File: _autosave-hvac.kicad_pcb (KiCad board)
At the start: 2 copper layers, 191.8 x 114.3 mm, 44 parts, among them IC1 ATMEGA328P-A, J1 PROGRAMMING HEADER, J2 SERIAL PORT, J3 POWER_INPUT, SW1 SPST, SW2 SPST, SW3 SPST, U1 MIC5225, U2 MOSFET_N, U3 MOSFET_N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

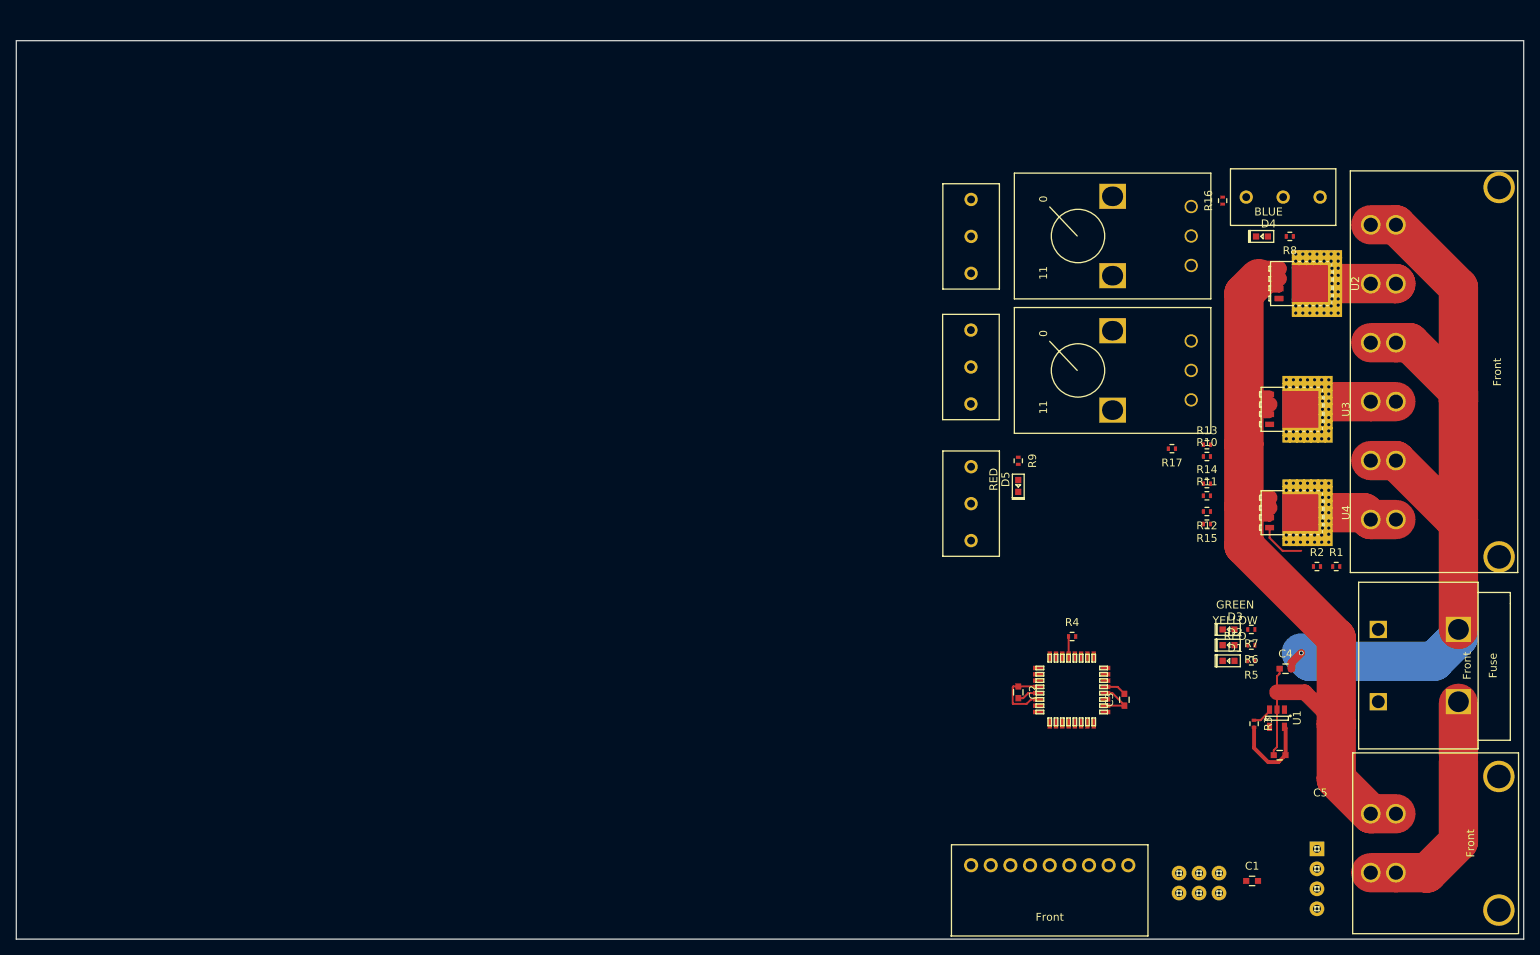
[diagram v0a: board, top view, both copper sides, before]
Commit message: Create hole footprint and route a few small things
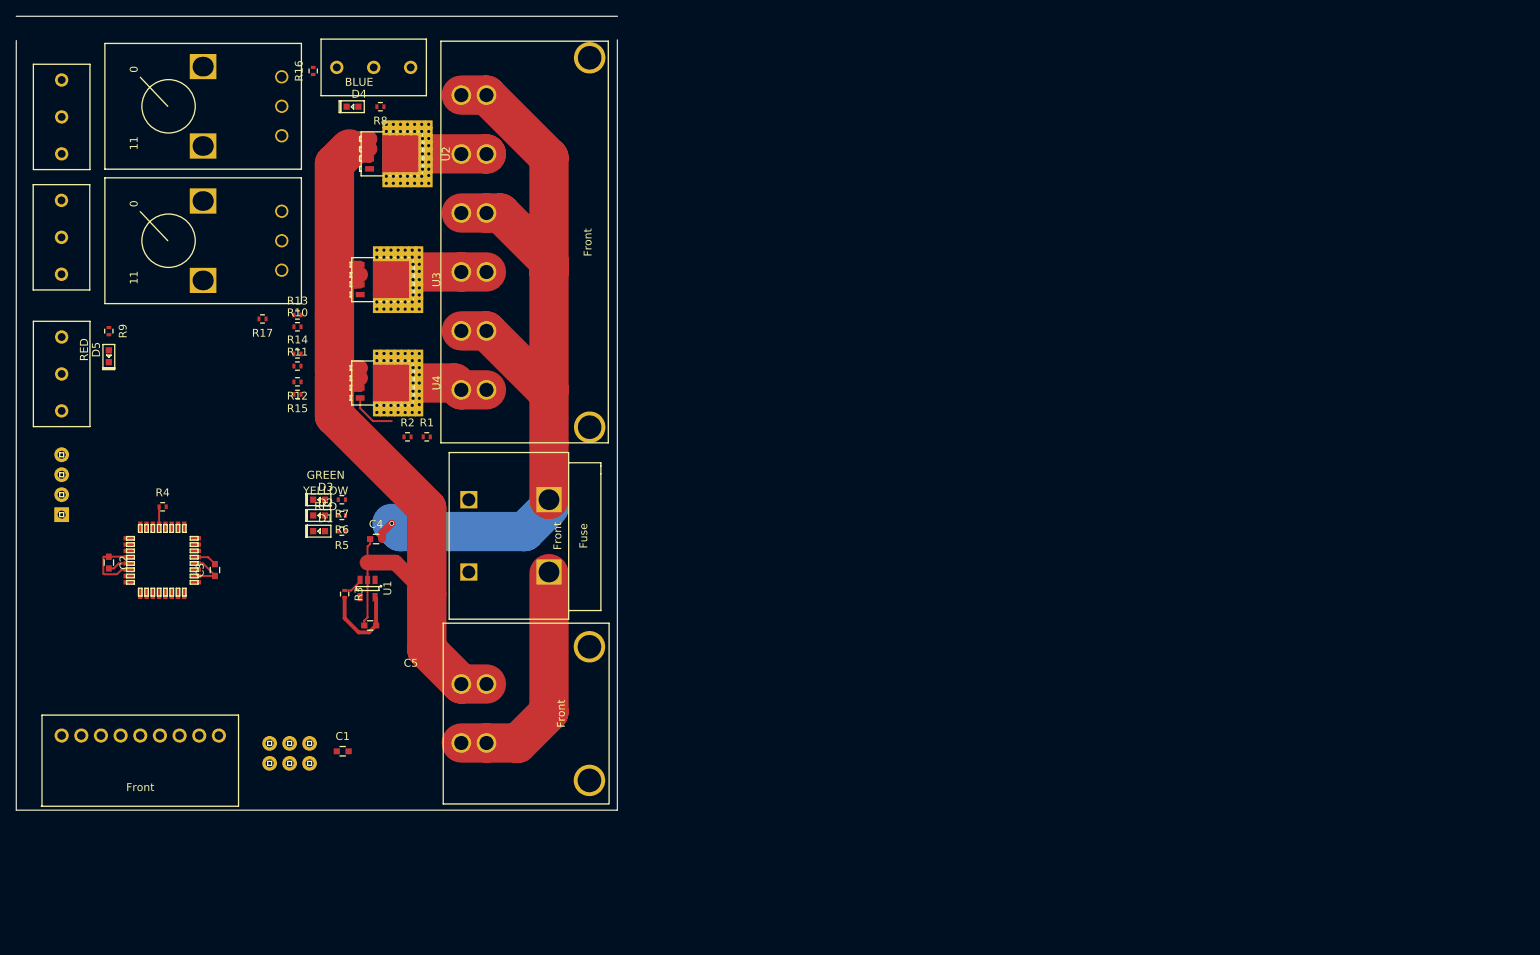
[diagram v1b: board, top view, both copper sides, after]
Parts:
- moved J2 165.3 mm to (55.3, 98.4), turned to 90 degrees
- moved J3 116.9 mm to (109.3, 123.7)
- moved JP1 116.9 mm to (109.3, 63.8)
- moved R17 116.9 mm to (80.8, 73.5)
- moved R8 116.9 mm to (95.8, 46.5)
- moved U3 116.9 mm to (96.1, 68.5)
- moved U4 116.9 mm to (96.1, 81.7)
- moved C1 116.9 mm to (91.0, 128.5)
- moved C2 116.9 mm to (61.3, 104.5)
- moved C3 116.9 mm to (74.8, 105.5)
- moved C4 116.9 mm to (95.3, 101.5)
- moved C5 116.9 mm to (94.5, 112.5)
- moved D1 116.9 mm to (88.0, 100.5)
- moved D2 116.9 mm to (88.0, 98.5)
- moved D3 116.9 mm to (88.0, 96.5)
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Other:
- board size 191.8 x 114.3 mm -> 76.5 x 101 mm
